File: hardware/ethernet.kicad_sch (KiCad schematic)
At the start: 38 parts, among them J5 HC-RJ45-055-7, J6 AUX_PWR, U2 SI3404-A-GMR

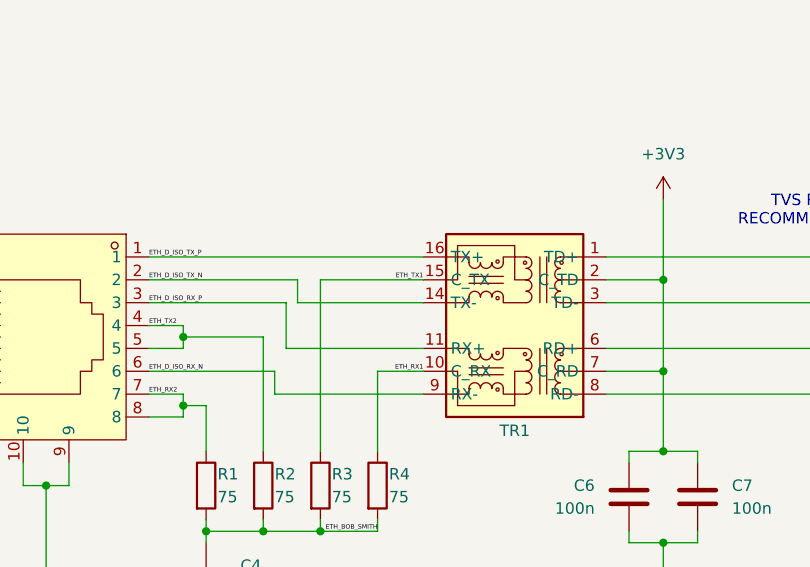
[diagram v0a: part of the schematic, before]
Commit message: Change pin layout to make Ethernet Routing nicer
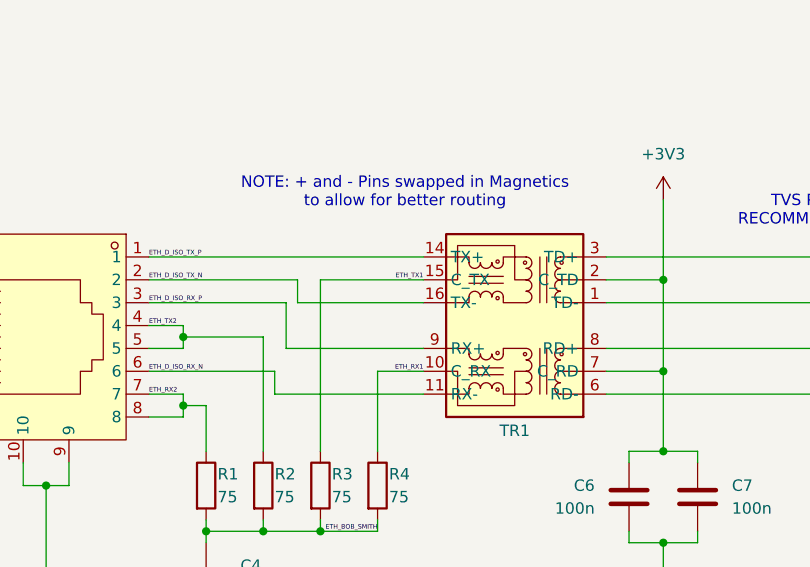
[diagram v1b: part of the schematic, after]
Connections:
- net ETH_D_ISO_RX_N: now also TR1.11 (RX-); no longer TR1.9 (RX-)
- net ETH_D_ISO_RX_P: now also TR1.9 (RX+); no longer TR1.11 (RX+)
- net ETH_D_ISO_TX_N: now also TR1.16 (TX-); no longer TR1.14 (TX-)
- net ETH_D_ISO_TX_P: now also TR1.14 (TX+); no longer TR1.16 (TX+)
- net ETH_D_RX_N: now also TR1.6 (RD-); no longer TR1.8 (RD-)
- net ETH_D_RX_P: now also TR1.8 (RD+); no longer TR1.6 (RD+)
- net ETH_D_TX_N: now also TR1.1 (TD-); no longer TR1.3 (TD-)
- net ETH_D_TX_P: now also TR1.3 (TD+); no longer TR1.1 (TD+)
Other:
- note added: "NOTE: + and - Pins swapped in Magnetics to allow for better routing"
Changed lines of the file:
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@@
+		)
+	)
+	(text "NOTE: + and - Pins swapped in Magnetics\nto allow for better routing"
+		(exclude_from_sim no)
+		(at 91.948 122.428 0)
+		(effects
+			(font
+				(size 1.27 1.27)
+			)
 		)
 	)

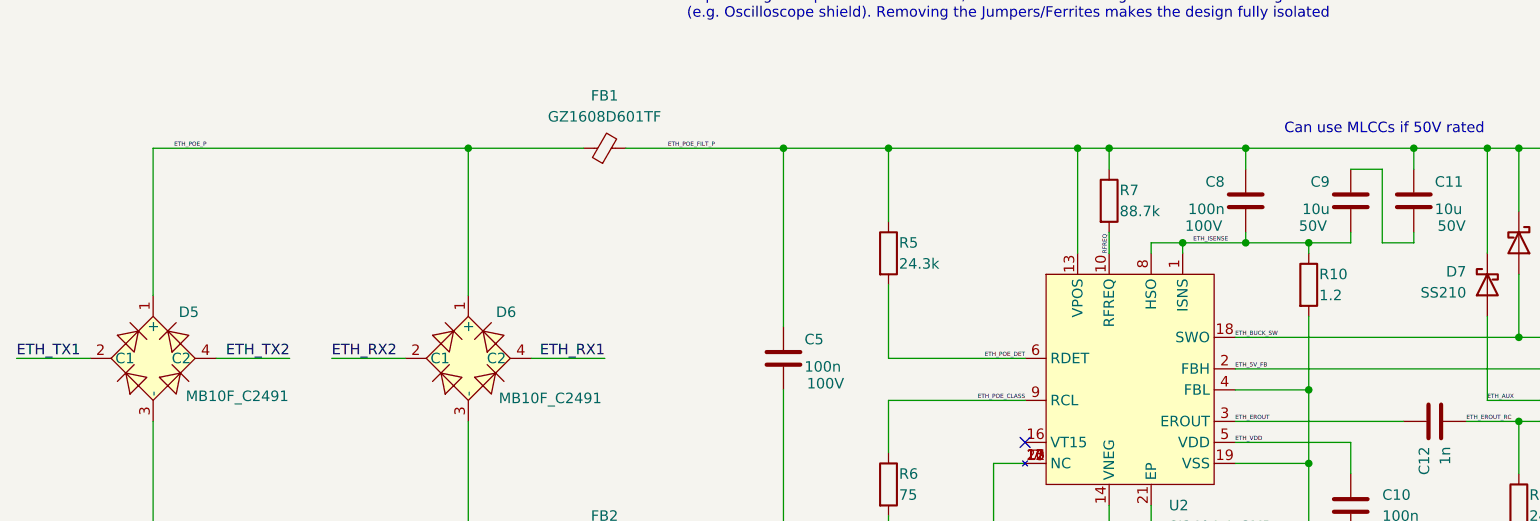
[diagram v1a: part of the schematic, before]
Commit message: ISO ETH Section Done
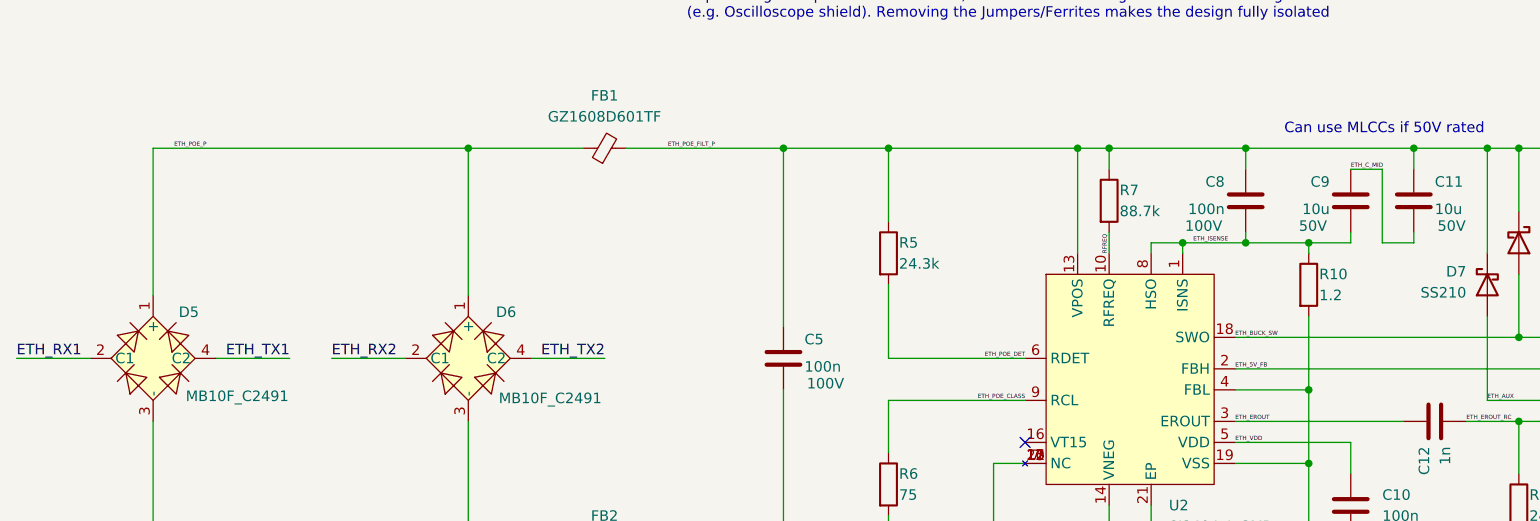
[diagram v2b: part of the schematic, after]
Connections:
- net ETH_RX1: now also D5.2 (C1); no longer D6.4 (C2)
- net ETH_TX1: now also D5.4 (C2); no longer D5.2 (C1)
- net ETH_TX2: now also D6.4 (C2); no longer D5.4 (C2)
- net ETH_C_MID: now reaches C11.2, C9.1
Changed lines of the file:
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@@
 		)
 	)
-	(label "ETH_RX1"
+	(label "ETH_TX2"
 		(at 92.71 63.5 180)
 		(effects
@@
 		)
 	)
-	(label "ETH_TX1"
+	(label "ETH_RX1"
 		(at 21.59 63.5 0)
 		(effects
@@
 		)
 	)
+	(label "ETH_C_MID"
+		(at 182.88 40.64 0)
+		(effects
+			(font
+				(size 0.508 0.508)
+				(color 132 132 132 1)
+			)
+			(justify left bottom)
+		)
+	)
 	(label "ETH_TX2"
 		(at 63.5 137.16 0)
@@
 		)
 	)
-	(label "ETH_TX2"
+	(label "ETH_TX1"
 		(at 54.61 63.5 180)
 		(effects

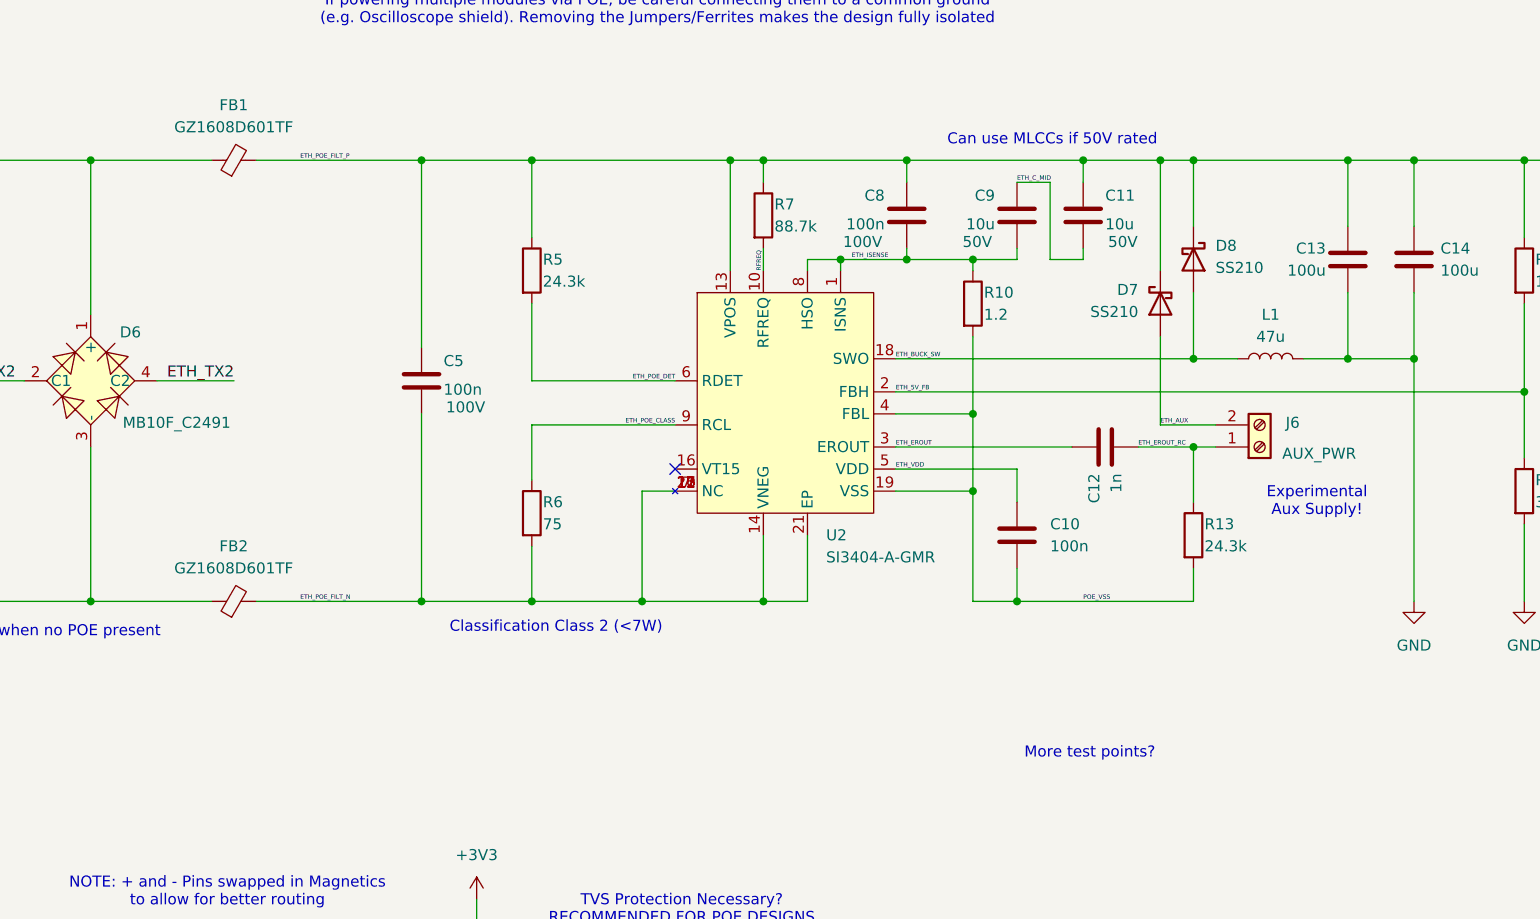
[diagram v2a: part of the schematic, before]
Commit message: Fix aux pwr oops
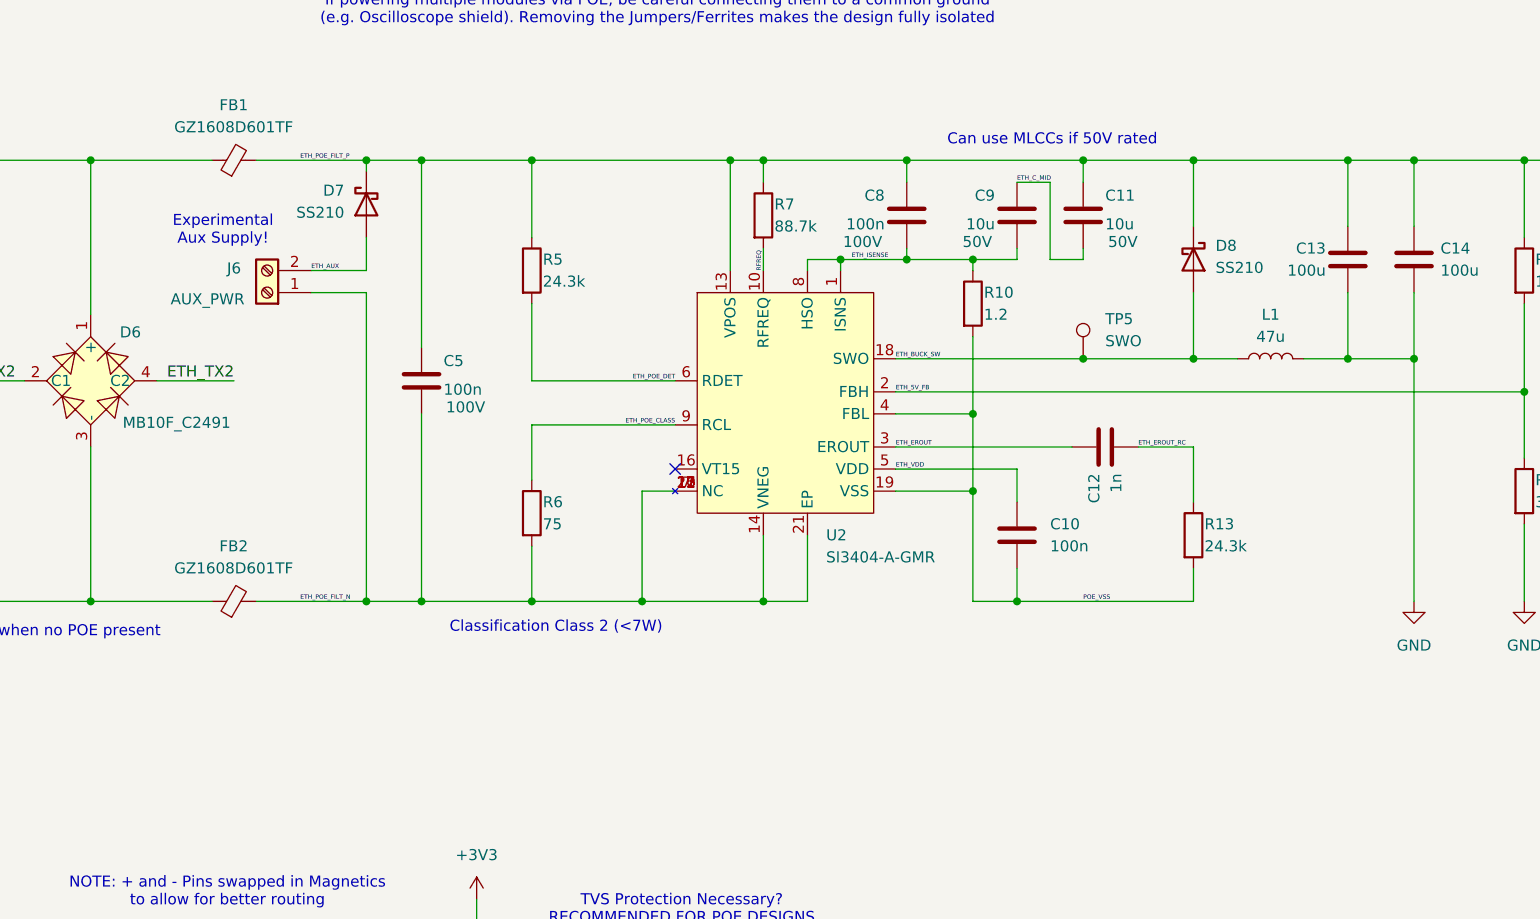
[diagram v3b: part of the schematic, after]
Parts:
- added TP5: SWO, TestPoint:TestPoint_Pad_D1.5mm, symbol Connector:TestPoint
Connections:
- net ETH_BUCK_SW: now also TP5.1
- net ETH_EROUT_RC: no longer J6.1 (Pin_1)
- net ETH_POE_FILT_N: now also J6.1 (Pin_1)
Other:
- note removed: "More test points?"
- moved on the sheet: D7, J6
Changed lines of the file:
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@@
 	(text "Experimental\nAux Supply!"
 		(exclude_from_sim no)
-		(at 217.424 77.47 0)
+		(at 91.44 46.228 0)
 		(effects
 			(font
@@
 		)
 	)
-	(text "More test points?"
-		(exclude_from_sim no)
-		(at 191.262 106.426 0)
-		(effects
-			(font
-				(size 1.27 1.27)
-			)
-		)
-	)
 	(text "NOTE: This is a non-isolated POE design to keep costs manageable:\nIf powering multiple modules via POE, be careful connecting them to a common ground\n(e.g. Oscilloscope shield). Removing the Jumpers/Ferrites makes the design fully isolated"
 		(exclude_from_sim no)
@@
 	)
 	(junction
-		(at 199.39 38.1)
+		(at 190.5 38.1)
 		(diameter 0)
 		(color 0 0 0 0)
 	)
 	(junction
-		(at 190.5 38.1)
+		(at 114.3 38.1)
 		(diameter 0)
 		(color 0 0 0 0)
 	)
 	(junction
-		(at 114.3 38.1)
+		(at 190.5 60.96)
 		(diameter 0)
 		(color 0 0 0 0)
@@
 	)
 	(junction
+		(at 107.95 88.9)
+		(diameter 0)
+		(color 0 0 0 0)
+	)
+	(junction
 		(at 241.3 38.1)
 		(diameter 0)
@@
 	)
 	(junction
-		(at 203.2 71.12)
+		(at 107.95 38.1)
 		(diameter 0)
 		(color 0 0 0 0)
@@
 	(wire
 		(pts
-			(xy 199.39 38.1) (xy 203.2 38.1)
-		)
-		(stroke
-			(width 0)
-			(type default)
-		)
-	)
-	(wire
-		(pts
 			(xy 127 68.58) (xy 127 74.93)
 		)
@@
 	(wire
 		(pts
+			(xy 107.95 50.8) (xy 107.95 46.99)
+		)
+		(stroke
+			(width 0)
+			(type default)
+		)
+	)
+	(wire
+		(pts
 			(xy 228.6 53.34) (xy 228.6 60.96)
 		)
@@
 	(wire
 		(pts
-			(xy 190.5 38.1) (xy 199.39 38.1)
+			(xy 190.5 38.1) (xy 203.2 38.1)
 		)
 		(stroke
@@
 	(wire
 		(pts
-			(xy 168.91 60.96) (xy 203.2 60.96)
+			(xy 168.91 60.96) (xy 190.5 60.96)
 		)
 		(stroke
@@
 	(wire
 		(pts
-			(xy 63.5 129.54) (xy 93.98 129.54)
+			(xy 153.67 38.1) (xy 170.18 38.1)
 		)
 		(stroke
@@
 	(wire
 		(pts
-			(xy 199.39 68.58) (xy 199.39 58.42)
+			(xy 63.5 129.54) (xy 93.98 129.54)
 		)
 		(stroke
@@
 	(wire
 		(pts
-			(xy 254 46.99) (xy 254 38.1)
+			(xy 107.95 38.1) (xy 114.3 38.1)
 		)
 		(stroke
@@
 	(wire
 		(pts
-			(xy 116.84 151.13) (xy 120.65 151.13)
+			(xy 254 46.99) (xy 254 38.1)
 		)
 		(stroke
@@
 	(wire
 		(pts
-			(xy 95.25 38.1) (xy 114.3 38.1)
+			(xy 116.84 151.13) (xy 120.65 151.13)
 		)
 		(stroke
@@
 	(wire
 		(pts
-			(xy 203.2 85.09) (xy 203.2 88.9)
+			(xy 95.25 38.1) (xy 107.95 38.1)
 		)
 		(stroke
@@
 	(wire
 		(pts
-			(xy 203.2 71.12) (xy 205.74 71.12)
+			(xy 203.2 85.09) (xy 203.2 88.9)
 		)
 		(stroke
@@
 	(wire
 		(pts
+			(xy 107.95 53.34) (xy 107.95 88.9)
+		)
+		(stroke
+			(width 0)
+			(type default)
+		)
+	)
+	(wire
+		(pts
 			(xy 143.51 68.58) (xy 127 68.58)
 		)
@@
 	(wire
 		(pts
-			(xy 114.3 134.62) (xy 139.7 134.62)
+			(xy 114.3 38.1) (xy 127 38.1)
 		)
 		(stroke
@@
 	(wire
 		(pts
-			(xy 220.98 60.96) (xy 215.9 60.96)
+			(xy 114.3 134.62) (xy 139.7 134.62)
 		)
 		(stroke
@@
 	(wire
 		(pts
-			(xy 203.2 88.9) (xy 182.88 88.9)
+			(xy 220.98 60.96) (xy 215.9 60.96)
 		)
 		(stroke
@@
 	(wire
 		(pts
-			(xy 153.67 38.1) (xy 170.18 38.1)
+			(xy 203.2 88.9) (xy 182.88 88.9)
 		)
 		(stroke
@@
 	(wire
 		(pts
-			(xy 95.25 88.9) (xy 114.3 88.9)
+			(xy 95.25 88.9) (xy 107.95 88.9)
 		)
 		(stroke
@@
 	(wire
 		(pts
-			(xy 205.74 68.58) (xy 199.39 68.58)
-		)
-		(stroke
-			(width 0)
-			(type default)
-		)
-	)
-	(wire
-		(pts
 			(xy 220.98 60.96) (xy 228.6 60.96)
 		)
@@
 	(wire
 		(pts
+			(xy 101.6 50.8) (xy 107.95 50.8)
+		)
+		(stroke
+			(width 0)
+			(type default)
+		)
+	)
+	(wire
+		(pts
+			(xy 190.5 60.96) (xy 203.2 60.96)
+		)
+		(stroke
+			(width 0)
+			(type default)
+		)
+	)
+	(wire
+		(pts
 			(xy 190.5 48.26) (xy 190.5 49.53)
 		)
@@
 	(wire
 		(pts
-			(xy 77.47 144.78) (xy 77.47 142.24)
+			(xy 107.95 88.9) (xy 114.3 88.9)
 		)
 		(stroke
@@
 	(wire
 		(pts
-			(xy 114.3 38.1) (xy 127 38.1)
+			(xy 77.47 144.78) (xy 77.47 142.24)
 		)
 		(stroke
@@
 	(wire
 		(pts
-			(xy 199.39 38.1) (xy 199.39 50.8)
+			(xy 107.95 38.1) (xy 107.95 39.37)
 		)
 		(stroke
@@
 	(wire
 		(pts
+			(xy 101.6 53.34) (xy 107.95 53.34)
+		)
+		(stroke
+			(width 0)
+			(type default)
+		)
+	)
+	(wire
+		(pts
 			(xy 120.65 132.08) (xy 120.65 142.24)
 		)
@@
 	)
 	(label "ETH_AUX"
-		(at 199.39 68.58 0)
+		(at 101.6 50.8 0)
 		(effects
 			(font
@@
 	(symbol
 		(lib_id "Device:D_Schottky")
-		(at 199.39 54.61 90)
+		(at 107.95 43.18 90)
 		(mirror x)
 		(unit 1)
@@
 		(dnp no)
 		(property "Reference" "D7"
-			(at 196.85 53.0224 90)
+			(at 105.41 41.5924 90)
 			(effects
 				(font
@@
 		)
 		(property "Value" "SS210"
-			(at 196.85 55.5624 90)
+			(at 105.41 44.1324 90)
 			(effects
 				(font
@@
 		)
 		(property "Footprint" "Diode_SMD:D_SMA"
-			(at 199.39 54.61 0)
+			(at 107.95 43.18 0)
 			(effects
 				(font
@@
 		)
 		(property "Datasheet" "~"
-			(at 199.39 54.61 0)
+			(at 107.95 43.18 0)
 			(effects
 				(font
@@
 		)
 		(property "Description" "Schottky diode"
-			(at 199.39 54.61 0)
+			(at 107.95 43.18 0)
 			(effects
 				(font
@@
 		)
 		(property "LCSC Part" "C14996"
-			(at 199.39 54.61 90)
+			(at 107.95 43.18 90)
 			(effects
 				(font
@@
 	)
 	(symbol
+		(lib_id "Connector:TestPoint")
+		(at 190.5 60.96 0)
+		(unit 1)
+		(exclude_from_sim no)
+		(in_bom yes)
+		(on_board yes)
+		(dnp no)
+		(fields_autoplaced yes)
+		(property "Reference" "TP5"
+			(at 193.04 56.3879 0)
+			(effects
+				(font
+					(size 1.27 1.27)
+				)
+				(justify left)
+			)
+		)
+		(property "Value" "SWO"
+			(at 193.04 58.9279 0)
+			(effects
+				(font
+					(size 1.27 1.27)
+				)
+				(justify left)
+			)
+		)
+		(property "Footprint" "TestPoint:TestPoint_Pad_D1.5mm"
+			(at 195.58 60.96 0)
+			(effects
+				(font
+					(size 1.27 1.27)
+				)
+				(hide yes)
+			)
+		)
+		(property "Datasheet" "~"
+			(at 195.58 60.96 0)
+			(effects
+				(font
+					(size 1.27 1.27)
+				)
+				(hide yes)
+			)
+		)
+		(property "Description" "test point"
+			(at 190.5 60.96 0)
+			(effects
+				(font
+					(size 1.27 1.27)
+				)
+				(hide yes)
+			)
+		)
+		(pin "1"
+		)
+		(instances
+			(project "uPTP"
+				(path "/c29659fd-9e8d-4714-a690-4e74e6e849c2/8e64a963-7181-4c69-8059-c99395347002"
+					(reference "TP5")
+					(unit 1)
+				)
+			)
+		)
+	)
+	(symbol
 		(lib_id "Device:R")
 		(at 127 78.74 0)
@@
 	(symbol
 		(lib_id "Connector:Screw_Terminal_01x02")
-		(at 210.82 71.12 0)
-		(mirror x)
+		(at 96.52 53.34 180)
 		(unit 1)
 		(exclude_from_sim no)
@@
 		(dnp no)
 		(property "Reference" "J6"
-			(at 214.63 68.326 0)
+			(at 92.71 50.546 0)
 			(effects
 				(font
@@
 		)
 		(property "Value" "AUX_PWR"
-			(at 217.678 71.882 0)
+			(at 89.662 54.102 0)
 			(effects
 				(font
@@
 		)
 		(property "Footprint" "TerminalBlock_Phoenix:TerminalBlock_Phoenix_MPT-0,5-2-2.54_1x02_P2.54mm_Horizontal"
-			(at 210.82 71.12 0)
+			(at 96.52 53.34 0)
 			(effects
 				(font
@@
 		)
 		(property "Datasheet" "~"
-			(at 210.82 71.12 0)
+			(at 96.52 53.34 0)
 			(effects
 				(font
@@
 		)
 		(property "Description" "Generic screw terminal, single row, 01x02, script generated (kicad-library-utils/schlib/autogen/connector/)"
-			(at 210.82 71.12 0)
+			(at 96.52 53.34 0)
 			(effects
 				(font

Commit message: Correct misunderstandings, mostly there
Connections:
- net ETH_ISENSE: now also J6.1 (Pin_1), R10.2; no longer C8.2, C9.2, R10.1
- net ETH_POE_FILT_N: no longer J6.1 (Pin_1)
- net POE_VSS: now also C8.2, C9.2, R10.1; no longer R10.2
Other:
- moved on the sheet: C11, C8, C9, D7, J6, R10

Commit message: Re-link rounded to be default
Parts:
- J6, TP5: now left out of the parts list
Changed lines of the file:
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@@
 		(unit 1)
 		(exclude_from_sim no)
-		(in_bom yes)
+		(in_bom no)
 		(on_board yes)
 		(dnp no)
@@
 		(unit 1)
 		(exclude_from_sim no)
-		(in_bom yes)
+		(in_bom no)
 		(on_board yes)
 		(dnp no)
